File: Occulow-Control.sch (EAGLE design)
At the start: 43 parts, among them T1 DMP3010LK3, T2 DMP3010LK3, T3 DMP3010LK3

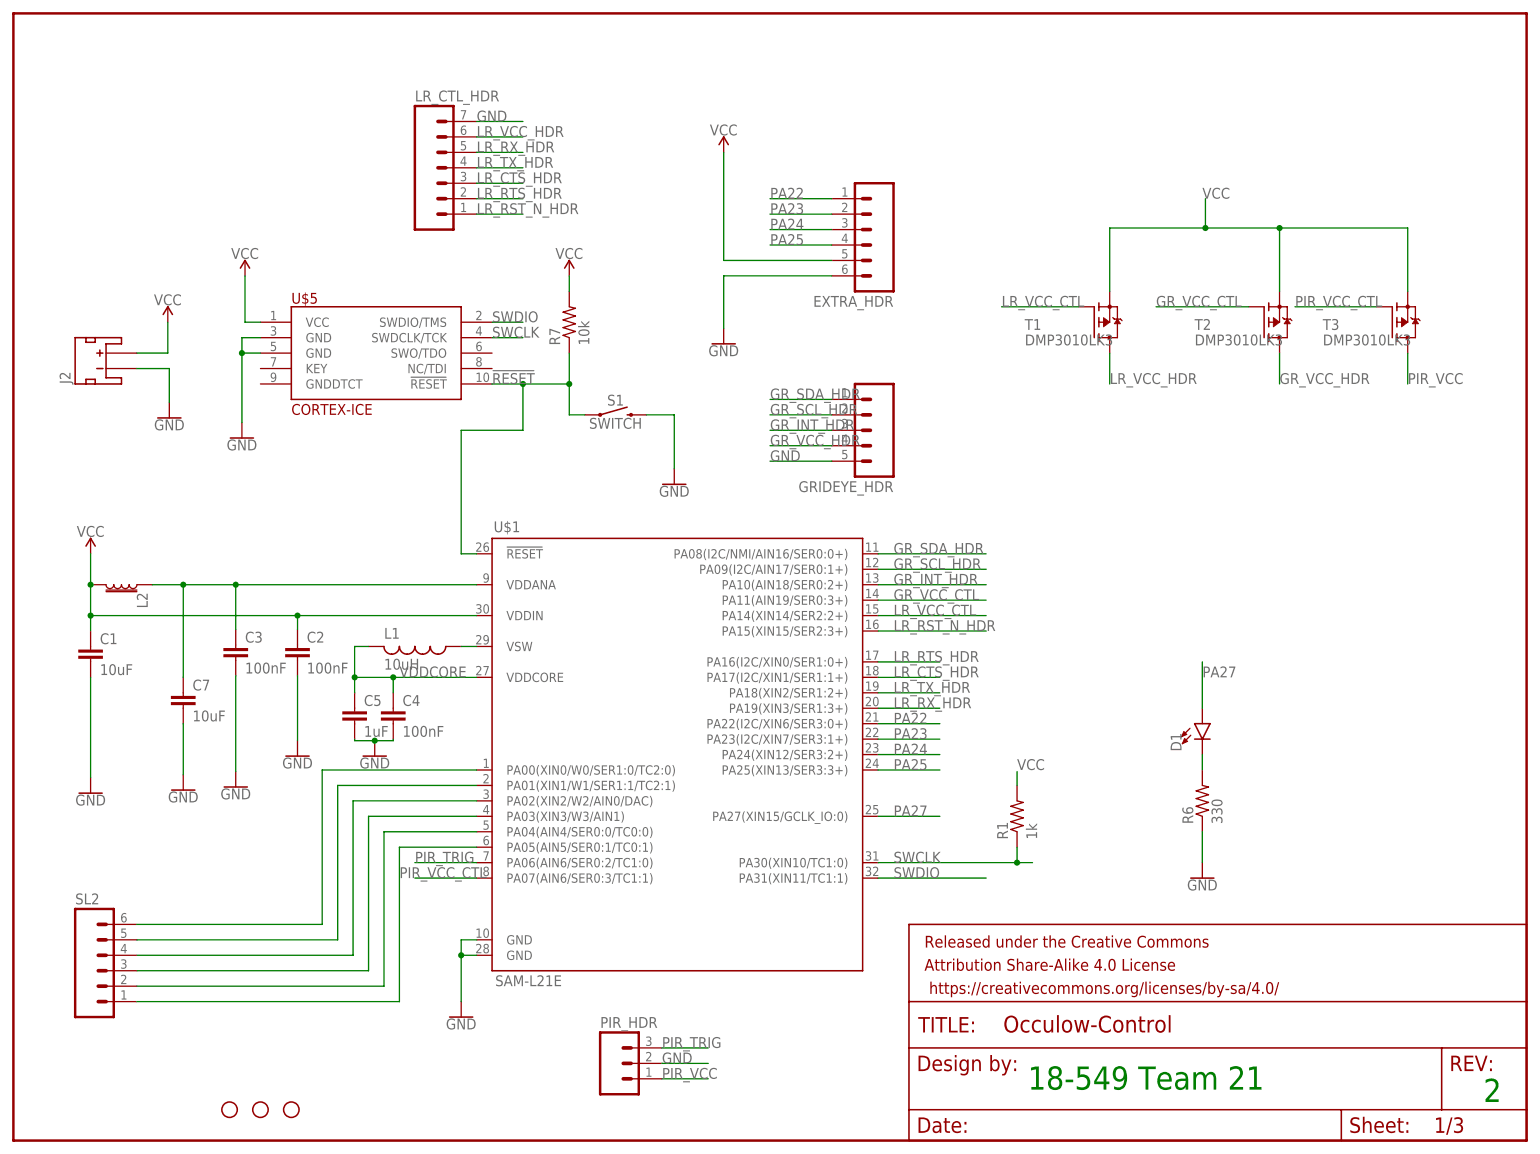
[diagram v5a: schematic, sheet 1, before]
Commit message: Replaced extra header with JTAG and i2c headers. Fixes #4
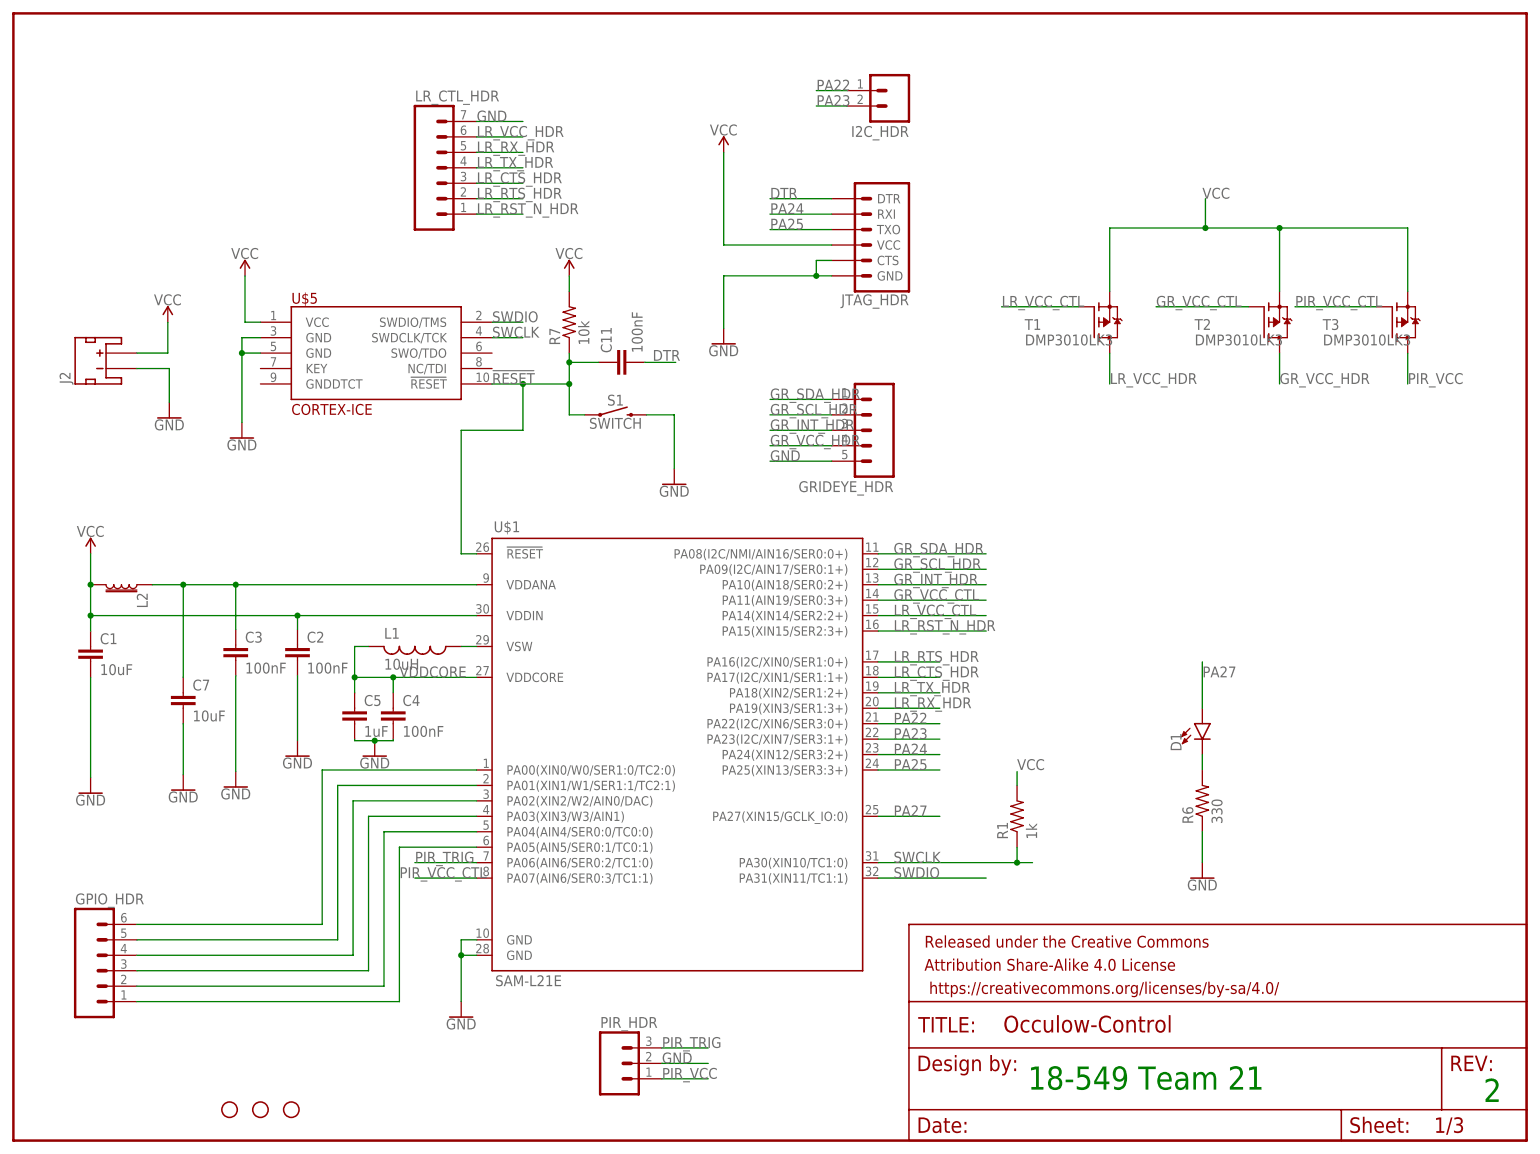
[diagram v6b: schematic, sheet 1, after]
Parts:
- removed EXTRA_HDR: (no value), con-amp-quick:M06
- added C11: 100nF, rcl:C-EUC1206
- added I2C_HDR: (no value), con-amp-quick:M02
- added JTAG_HDR: (no value), SparkFun-Connectors:6_PIN_SERIAL_TARGET
- renumbered SL2 to GPIO_HDR
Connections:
- new net DTR: C11.2, JTAG_HDR.DTR
- net !RESET: now also C11.1
- net GND: now also JTAG_HDR.CTS, JTAG_HDR.GND; no longer EXTRA_HDR.6
- net PA22: now also I2C_HDR.1; no longer EXTRA_HDR.1
- net PA23: now also I2C_HDR.2; no longer EXTRA_HDR.2
- net PA24: now also JTAG_HDR.RXI; no longer EXTRA_HDR.3
- net PA25: now also JTAG_HDR.TXO; no longer EXTRA_HDR.4
- net VCC: now also JTAG_HDR.VCC; no longer EXTRA_HDR.5
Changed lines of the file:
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@@
 <part name="SUPPLY6" library="SparkFun-PowerSymbols" deviceset="VCC" device=""/>
 <part name="GND11" library="SparkFun-PowerSymbols" deviceset="GND" device=""/>
-<part name="EXTRA_HDR" library="con-amp-quick" deviceset="M06" device=""/>
 <part name="L1" library="resistor" deviceset="L-US" device="L3225M" value="10uH"/>
 <part name="L2" library="SparkFun-Coils" deviceset="FERRITE_BEAD" device="-0603" value=""/>
@@
 <part name="GND4" library="SparkFun-PowerSymbols" deviceset="GND" device=""/>
 <part name="GND13" library="SparkFun-PowerSymbols" deviceset="GND" device=""/>
-<part name="SL2" library="con-amp-quick" deviceset="M06" device=""/>
+<part name="GPIO_HDR" library="con-amp-quick" deviceset="M06" device=""/>
 <part name="H1" library="SparkFun-Hardware" deviceset="STAND-OFF" device=""/>
 <part name="H2" library="SparkFun-Hardware" deviceset="STAND-OFF" device=""/>
@@
 <part name="SUPPLY2" library="SparkFun-PowerSymbols" deviceset="VCC" device=""/>
 <part name="GND6" library="SparkFun-PowerSymbols" deviceset="GND" device=""/>
+<part name="JTAG_HDR" library="SparkFun-Connectors" deviceset="6_PIN_SERIAL_TARGET" device=""/>
+<part name="C11" library="rcl" deviceset="C-EU" device="C1206" value="100nF"/>
+<part name="I2C_HDR" library="con-amp-quick" deviceset="M02" device=""/>
 </parts>
 <sheets>
@@
 <instance part="SUPPLY6" gate="G$1" x="25.4" y="134.62"/>
 <instance part="GND11" gate="1" x="25.654" y="118.872"/>
-<instance part="EXTRA_HDR" gate="G$1" x="139.7" y="149.86" rot="R180"/>
 <instance part="L1" gate="G$1" x="66.04" y="81.28" rot="R270"/>
 <instance part="L2" gate="G$1" x="17.78" y="91.44" rot="R270"/>
@@
 <instance part="GND4" gate="1" x="59.436" y="63.246"/>
 <instance part="GND13" gate="1" x="46.736" y="63.246"/>
-<instance part="SL2" gate="G$1" x="15.24" y="27.94"/>
+<instance part="GPIO_HDR" gate="G$1" x="15.24" y="27.94"/>
 <instance part="H1" gate="G$1" x="35.56" y="5.08"/>
 <instance part="H2" gate="G$1" x="40.64" y="5.08"/>
@@
 <instance part="SUPPLY2" gate="G$1" x="91.44" y="142.24"/>
 <instance part="GND6" gate="1" x="108.712" y="107.95"/>
+<instance part="JTAG_HDR" gate="G$1" x="139.7" y="149.86" rot="R180"/>
+<instance part="C11" gate="G$1" x="98.806" y="128.016" rot="R90"/>
+<instance part="I2C_HDR" gate="G$1" x="144.78" y="172.72" rot="R180"/>
 </instances>
 <busses>
@@
 <pinref part="GND10" gate="1" pin="GND"/>
 <wire x1="116.84" y1="142.24" x2="116.84" y2="133.604" width="0.1524" layer="91"/>
-<pinref part="EXTRA_HDR" gate="G$1" pin="6"/>
-<wire x1="134.62" y1="142.24" x2="116.84" y2="142.24" width="0.1524" layer="91"/>
+<wire x1="134.62" y1="142.24" x2="132.08" y2="142.24" width="0.1524" layer="91"/>
+<pinref part="JTAG_HDR" gate="G$1" pin="GND"/>
+<pinref part="JTAG_HDR" gate="G$1" pin="CTS"/>
+<wire x1="132.08" y1="142.24" x2="116.84" y2="142.24" width="0.1524" layer="91"/>
+<wire x1="134.62" y1="144.78" x2="132.08" y2="144.78" width="0.1524" layer="91"/>
+<wire x1="132.08" y1="144.78" x2="132.08" y2="142.24" width="0.1524" layer="91"/>
+<junction x="132.08" y="142.24"/>
 </segment>
 <segment>
@@
 </segment>
 <segment>
-<pinref part="EXTRA_HDR" gate="G$1" pin="5"/>
-<pinref part="SUPPLY5" gate="G$1" pin="VCC"/>
-<wire x1="134.62" y1="144.78" x2="116.84" y2="144.78" width="0.1524" layer="91"/>
-<wire x1="116.84" y1="144.78" x2="116.84" y2="162.56" width="0.1524" layer="91"/>
-</segment>
-<segment>
 <pinref part="R7" gate="G$1" pin="2"/>
 <pinref part="SUPPLY2" gate="G$1" pin="VCC"/>
 <wire x1="91.44" y1="139.7" x2="91.44" y2="142.24" width="0.1524" layer="91"/>
+</segment>
+<segment>
+<pinref part="JTAG_HDR" gate="G$1" pin="VCC"/>
+<pinref part="SUPPLY5" gate="G$1" pin="VCC"/>
+<wire x1="134.62" y1="147.32" x2="116.84" y2="147.32" width="0.1524" layer="91"/>
+<wire x1="116.84" y1="147.32" x2="116.84" y2="162.56" width="0.1524" layer="91"/>
 </segment>
 </net>
@@
 <pinref part="U$1" gate="G$1" pin="PA00(XIN0/W0/SER1:0/TC2:0)"/>
 <wire x1="50.8" y1="60.96" x2="76.2" y2="60.96" width="0.1524" layer="91"/>
-<pinref part="SL2" gate="G$1" pin="6"/>
+<pinref part="GPIO_HDR" gate="G$1" pin="6"/>
 </segment>
 </net>
@@
 <pinref part="U$1" gate="G$1" pin="PA01(XIN1/W1/SER1:1/TC2:1)"/>
 <wire x1="53.34" y1="58.42" x2="76.2" y2="58.42" width="0.1524" layer="91"/>
-<pinref part="SL2" gate="G$1" pin="5"/>
+<pinref part="GPIO_HDR" gate="G$1" pin="5"/>
 </segment>
 </net>
@@
 <pinref part="U$1" gate="G$1" pin="PA02(XIN2/W2/AIN0/DAC)"/>
 <wire x1="55.88" y1="55.88" x2="76.2" y2="55.88" width="0.1524" layer="91"/>
-<pinref part="SL2" gate="G$1" pin="4"/>
+<pinref part="GPIO_HDR" gate="G$1" pin="4"/>
 </segment>
 </net>
@@
 <pinref part="U$1" gate="G$1" pin="PA03(XIN3/W3/AIN1)"/>
 <wire x1="58.42" y1="53.34" x2="76.2" y2="53.34" width="0.1524" layer="91"/>
-<pinref part="SL2" gate="G$1" pin="3"/>
+<pinref part="GPIO_HDR" gate="G$1" pin="3"/>
 </segment>
 </net>
@@
 <pinref part="U$1" gate="G$1" pin="PA04(AIN4/SER0:0/TC0:0)"/>
 <wire x1="60.96" y1="50.8" x2="76.2" y2="50.8" width="0.1524" layer="91"/>
-<pinref part="SL2" gate="G$1" pin="2"/>
+<pinref part="GPIO_HDR" gate="G$1" pin="2"/>
 </segment>
 </net>
@@
 <pinref part="U$1" gate="G$1" pin="PA05(AIN5/SER0:1/TC0:1)"/>
 <wire x1="63.5" y1="48.26" x2="76.2" y2="48.26" width="0.1524" layer="91"/>
-<pinref part="SL2" gate="G$1" pin="1"/>
+<pinref part="GPIO_HDR" gate="G$1" pin="1"/>
 </segment>
 </net>
@@
 </segment>
 <segment>
-<pinref part="EXTRA_HDR" gate="G$1" pin="1"/>
-<wire x1="134.62" y1="154.94" x2="124.46" y2="154.94" width="0.1524" layer="91"/>
-<label x="124.46" y="154.94" size="1.778" layer="95"/>
+<pinref part="I2C_HDR" gate="G$1" pin="1"/>
+<wire x1="137.16" y1="172.72" x2="132.08" y2="172.72" width="0.1524" layer="91"/>
+<label x="132.08" y="172.72" size="1.778" layer="95"/>
 </segment>
 </net>
@@
 </segment>
 <segment>
-<pinref part="EXTRA_HDR" gate="G$1" pin="2"/>
-<wire x1="134.62" y1="152.4" x2="124.46" y2="152.4" width="0.1524" layer="91"/>
-<label x="124.46" y="152.4" size="1.778" layer="95"/>
+<pinref part="I2C_HDR" gate="G$1" pin="2"/>
+<wire x1="137.16" y1="170.18" x2="132.08" y2="170.18" width="0.1524" layer="91"/>
+<label x="132.08" y="170.18" size="1.778" layer="95"/>
 </segment>
 </net>
@@
 <wire x1="91.44" y1="124.46" x2="91.44" y2="119.38" width="0.1524" layer="91"/>
 <pinref part="R7" gate="G$1" pin="1"/>
-<wire x1="91.44" y1="124.46" x2="91.44" y2="129.54" width="0.1524" layer="91"/>
+<wire x1="91.44" y1="124.46" x2="91.44" y2="128.016" width="0.1524" layer="91"/>
 <junction x="91.44" y="124.46"/>
+<pinref part="C11" gate="G$1" pin="1"/>
+<wire x1="91.44" y1="128.016" x2="91.44" y2="129.54" width="0.1524" layer="91"/>
+<wire x1="96.266" y1="128.016" x2="91.44" y2="128.016" width="0.1524" layer="91"/>
+<junction x="91.44" y="128.016"/>
 </segment>
 </net>
@@
 </segment>
 <segment>
-<wire x1="134.62" y1="149.86" x2="124.46" y2="149.86" width="0.1524" layer="91"/>
-<label x="124.46" y="149.86" size="1.778" layer="95"/>
-<pinref part="EXTRA_HDR" gate="G$1" pin="3"/>
+<wire x1="134.62" y1="152.4" x2="124.46" y2="152.4" width="0.1524" layer="91"/>
+<label x="124.46" y="152.4" size="1.778" layer="95"/>
+<pinref part="JTAG_HDR" gate="G$1" pin="RXI"/>
 </segment>
 </net>
@@
 </segment>
 <segment>
-<pinref part="EXTRA_HDR" gate="G$1" pin="4"/>
-<wire x1="134.62" y1="147.32" x2="124.46" y2="147.32" width="0.1524" layer="91"/>
-<label x="124.46" y="147.32" size="1.778" layer="95"/>
+<wire x1="134.62" y1="149.86" x2="124.46" y2="149.86" width="0.1524" layer="91"/>
+<label x="124.46" y="149.86" size="1.778" layer="95"/>
+<pinref part="JTAG_HDR" gate="G$1" pin="TXO"/>
 </segment>
 </net>
@@
 </segment>
 </net>
+<net name="DTR" class="0">
+<segment>
+<wire x1="134.62" y1="154.94" x2="127" y2="154.94" width="0.1524" layer="91"/>
+<label x="124.46" y="154.94" size="1.778" layer="95"/>
+<pinref part="JTAG_HDR" gate="G$1" pin="DTR"/>
+<wire x1="127" y1="154.94" x2="124.46" y2="154.94" width="0.1524" layer="91"/>
+</segment>
+<segment>
+<pinref part="C11" gate="G$1" pin="2"/>
+<wire x1="103.886" y1="128.016" x2="108.966" y2="128.016" width="0.1524" layer="91"/>
+<label x="105.156" y="128.27" size="1.778" layer="95"/>
+</segment>
+</net>

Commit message: Created 2 wire trap lib, placed in schematic
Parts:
- removed J2: (no value), SparkFun-Connectors:JST_2MM_MALE
- added U$7: MINI-LITE-TRAP, lite-trap:MINI-LITE-TRAP
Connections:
- net GND: now also U$7.2; no longer J2.-
- net VCC: now also U$7.1; no longer J2.+
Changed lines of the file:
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@@
 <?xml version="1.0" encoding="utf-8"?>
 <!DOCTYPE eagle SYSTEM "eagle.dtd">
-<eagle version="8.0.2">
+<eagle version="8.1.0">
 <drawing>
 <settings>
@@
 <part name="SUPPLY5" library="SparkFun-PowerSymbols" deviceset="VCC" device=""/>
 <part name="GND10" library="SparkFun-PowerSymbols" deviceset="GND" device=""/>
-<part name="J2" library="SparkFun-Connectors" deviceset="JST_2MM_MALE" device=""/>
 <part name="SUPPLY6" library="SparkFun-PowerSymbols" deviceset="VCC" device=""/>
 <part name="GND11" library="SparkFun-PowerSymbols" deviceset="GND" device=""/>
@@
 <part name="C11" library="rcl" deviceset="C-EU" device="C1206" value="100nF"/>
 <part name="I2C_HDR" library="con-amp-quick" deviceset="M02" device=""/>
+<part name="U$7" library="lite-trap" deviceset="MINI-LITE-TRAP" device=""/>
 </parts>
 <sheets>
@@
 <instance part="SUPPLY5" gate="G$1" x="116.84" y="162.56"/>
 <instance part="GND10" gate="1" x="116.84" y="131.064"/>
-<instance part="J2" gate="G$1" x="15.24" y="127" rot="R90"/>
 <instance part="SUPPLY6" gate="G$1" x="25.4" y="134.62"/>
 <instance part="GND11" gate="1" x="25.654" y="118.872"/>
@@
 <instance part="C11" gate="G$1" x="98.806" y="128.016" rot="R90"/>
 <instance part="I2C_HDR" gate="G$1" x="144.78" y="172.72" rot="R180"/>
+<instance part="U$7" gate="G$1" x="10.16" y="127"/>
 </instances>
 <busses>
@@
 <pinref part="U$5" gate="G$1" pin="GND@3"/>
 <pinref part="U$5" gate="G$1" pin="GND@5"/>
-</segment>
-<segment>
-<pinref part="J2" gate="G$1" pin="-"/>
-<pinref part="GND11" gate="1" pin="GND"/>
-<wire x1="20.32" y1="127" x2="25.654" y2="127" width="0.1524" layer="91"/>
-<wire x1="25.654" y1="127" x2="25.654" y2="121.412" width="0.1524" layer="91"/>
 </segment>
 <segment>
@@
 <wire x1="108.712" y1="119.38" x2="108.712" y2="110.49" width="0.1524" layer="91"/>
 </segment>
+<segment>
+<pinref part="U$7" gate="G$1" pin="2"/>
+<pinref part="GND11" gate="1" pin="GND"/>
+<wire x1="17.78" y1="124.46" x2="25.654" y2="124.46" width="0.1524" layer="91"/>
+<wire x1="25.654" y1="124.46" x2="25.654" y2="121.412" width="0.1524" layer="91"/>
+</segment>
 </net>
 <net name="VCC" class="0">
@@
 <wire x1="38.1" y1="134.62" x2="38.1" y2="142.24" width="0.1524" layer="91"/>
 <pinref part="U$5" gate="G$1" pin="VCC"/>
-</segment>
-<segment>
-<pinref part="J2" gate="G$1" pin="+"/>
-<pinref part="SUPPLY6" gate="G$1" pin="VCC"/>
-<wire x1="20.32" y1="129.54" x2="25.4" y2="129.54" width="0.1524" layer="91"/>
-<wire x1="25.4" y1="129.54" x2="25.4" y2="134.62" width="0.1524" layer="91"/>
 </segment>
 <segment>
@@
 <wire x1="134.62" y1="147.32" x2="116.84" y2="147.32" width="0.1524" layer="91"/>
 <wire x1="116.84" y1="147.32" x2="116.84" y2="162.56" width="0.1524" layer="91"/>
+</segment>
+<segment>
+<pinref part="U$7" gate="G$1" pin="1"/>
+<pinref part="SUPPLY6" gate="G$1" pin="VCC"/>
+<wire x1="17.78" y1="129.54" x2="25.4" y2="129.54" width="0.1524" layer="91"/>
+<wire x1="25.4" y1="129.54" x2="25.4" y2="134.62" width="0.1524" layer="91"/>
 </segment>
 </net>
@@
 </nets>
 </sheet>
+<sheet>
+<plain>
+</plain>
+<instances>
+</instances>
+<busses>
+</busses>
+<nets>
+</nets>
+</sheet>
